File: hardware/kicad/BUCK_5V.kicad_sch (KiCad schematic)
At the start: 0 parts

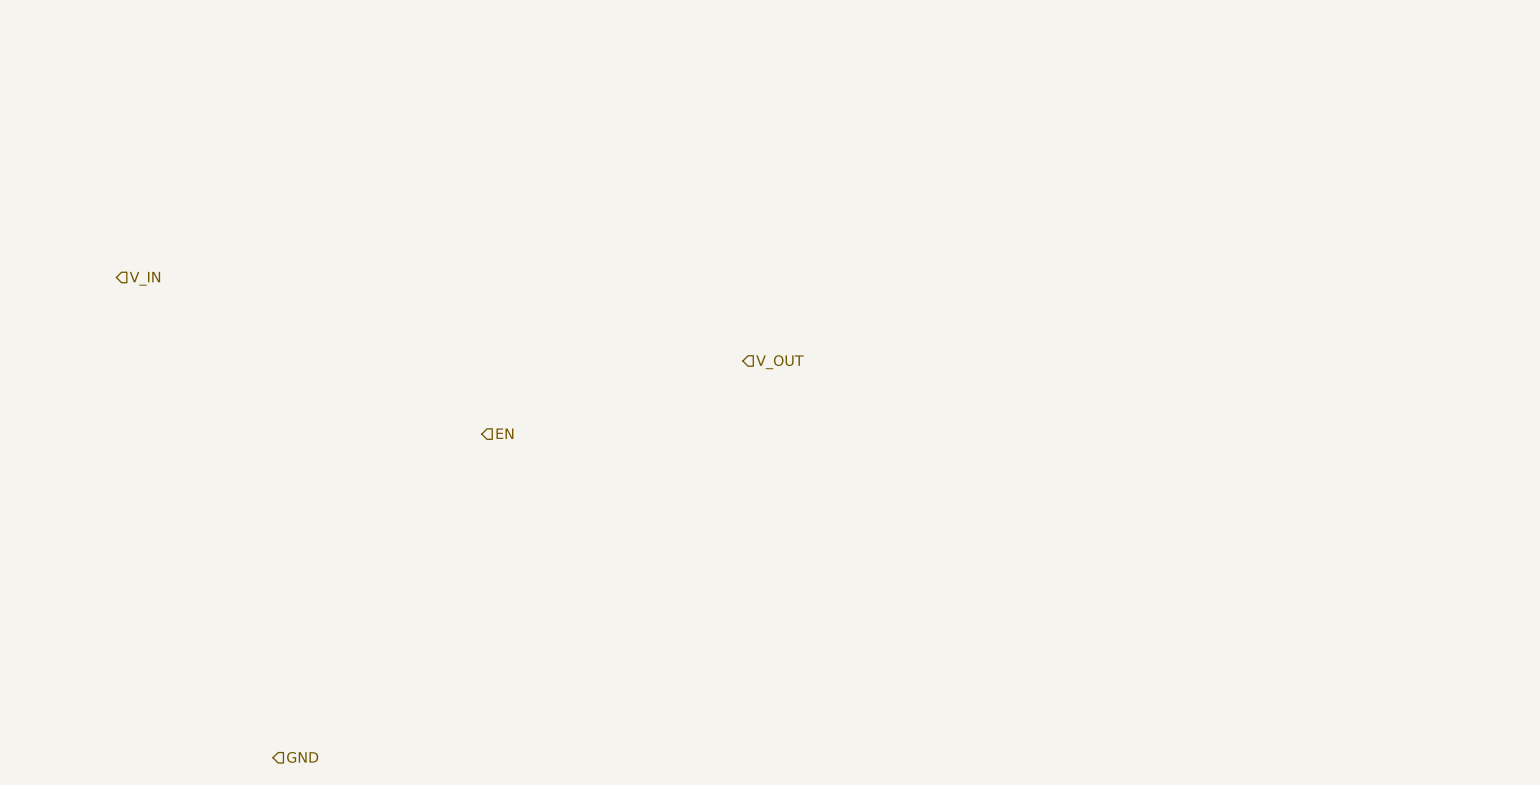
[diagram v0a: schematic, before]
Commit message: feat: added buck 12-5 & 12-3V3 layouts
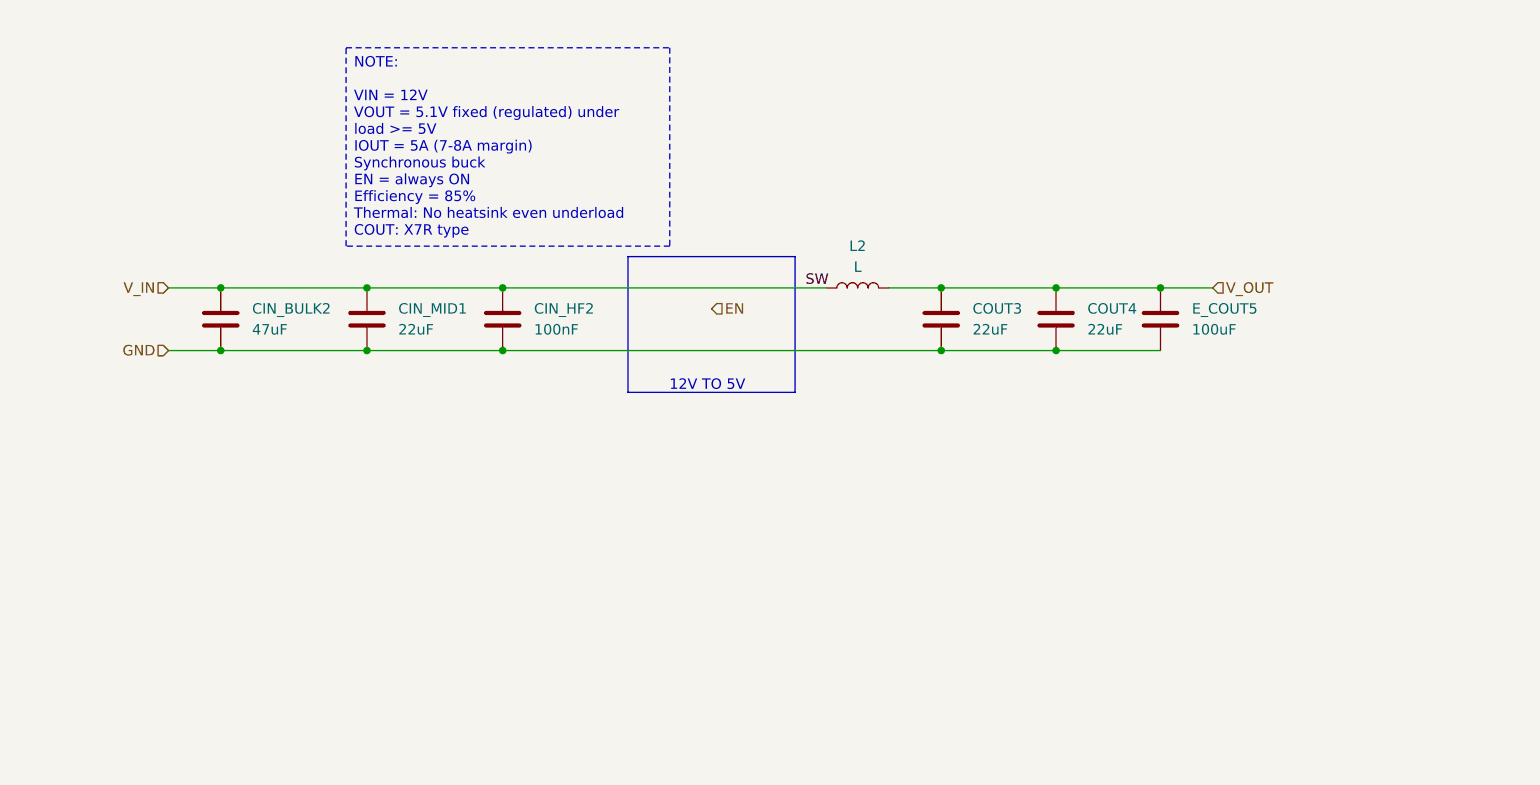
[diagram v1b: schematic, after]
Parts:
- added CIN_BULK2: 47uF, symbol Device:C
- added CIN_HF2: 100nF, symbol Device:C
- added CIN_MID1, COUT3, COUT4: 22uF, symbol Device:C
- added E_COUT5: 100uF, symbol Device:C
- added L2: L, symbol Device:L
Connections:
- net GND: now also CIN_BULK2.2, CIN_HF2.2, CIN_MID1.2, COUT3.2, COUT4.2, E_COUT5.2
- net V_IN: now also CIN_BULK2.1, CIN_HF2.1, CIN_MID1.1, L2.1
- net V_OUT: now also COUT3.1, COUT4.1, E_COUT5.1, L2.2
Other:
- note added: "12V TO 5V"

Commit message: feat: mcu interfaces & motor connections
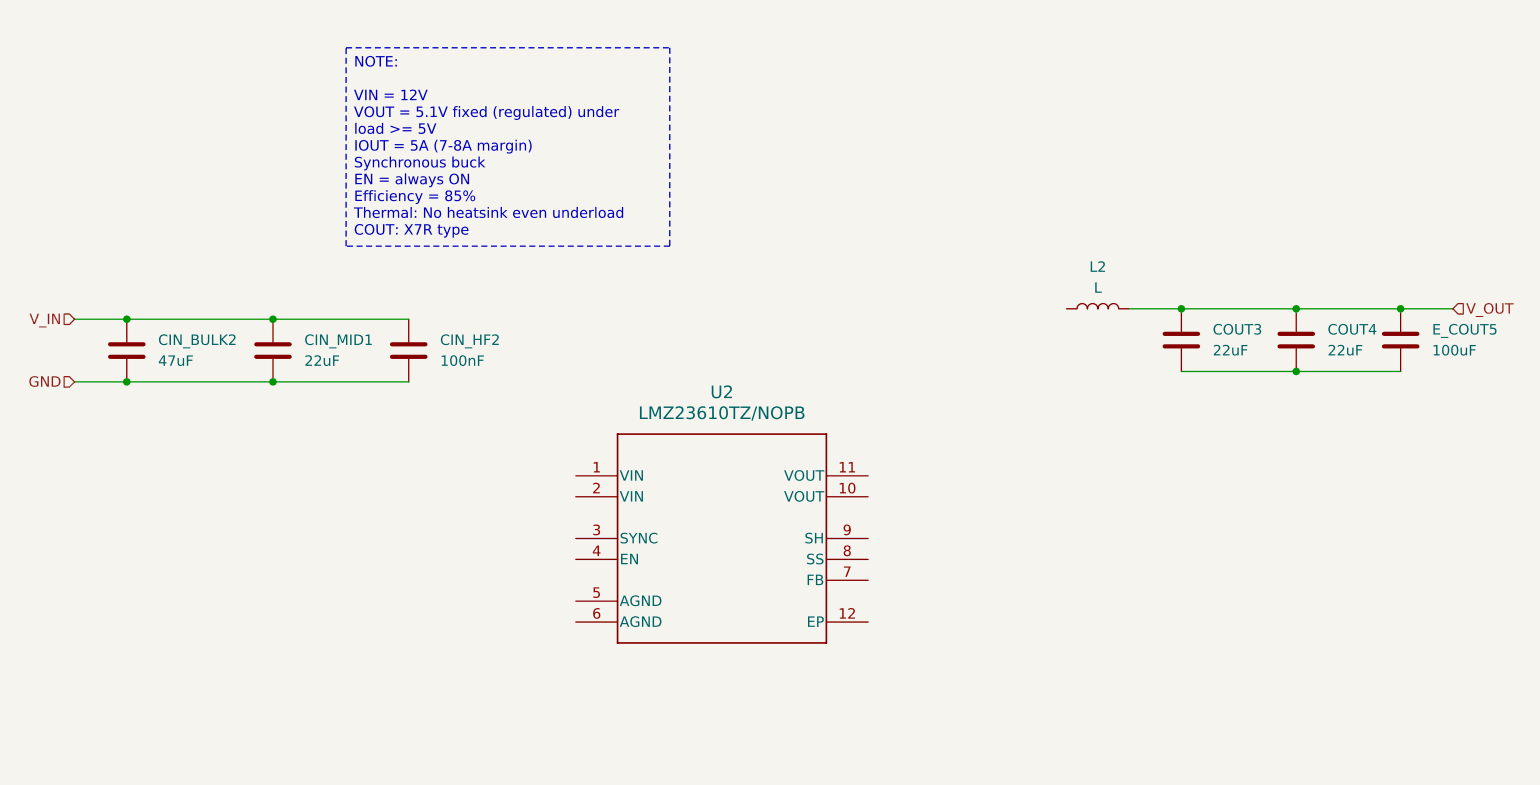
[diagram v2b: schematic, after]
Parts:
- added U2: LMZ23610TZ/NOPB, NDY0011A_N, symbol LMZ23610:LMZ23610TZ_NOPB
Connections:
- net GND: no longer COUT3.2, COUT4.2, E_COUT5.2
- net V_IN: no longer L2.1
- new net: COUT3.2, COUT4.2, E_COUT5.2
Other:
- note removed: "12V TO 5V"
- moved on the sheet: CIN_BULK2, CIN_HF2, CIN_MID1, COUT3, COUT4, E_COUT5, L2

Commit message: fix: error fixing & connection config
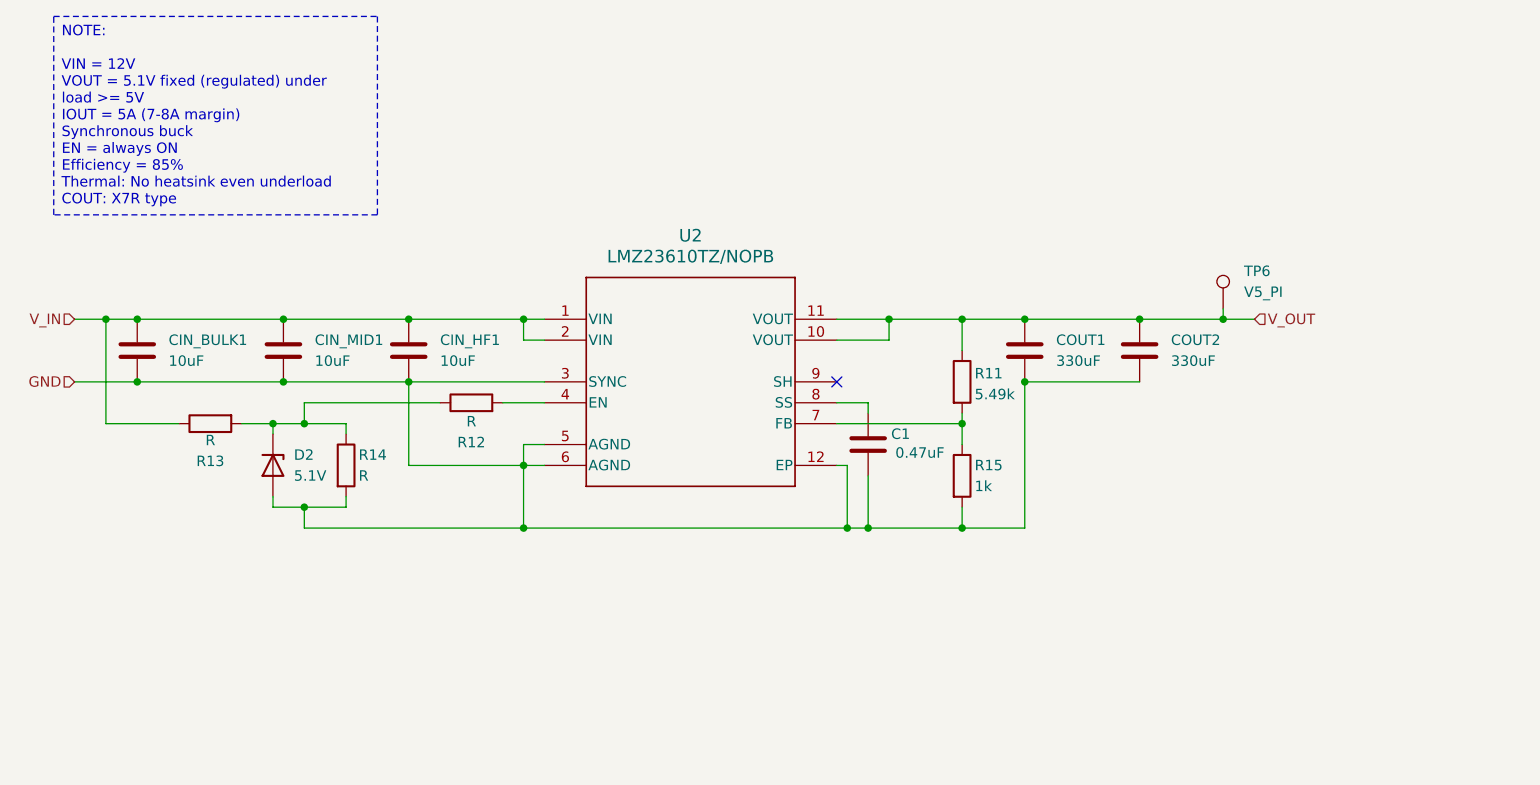
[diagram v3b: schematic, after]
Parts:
- removed E_COUT5: 100uF, symbol Device:C
- removed L2: L, symbol Device:L
- added C1: 0.47uF, symbol Device:C
- added D2: 5.1V, symbol Device:D_Zener
- added R11: 5.49k, symbol Device:R
- added R12, R13, R14: R, symbol Device:R
- added R15: 1k, symbol Device:R
- added TP6: V5_PI, symbol Connector:TestPoint
- CIN_BULK1: renamed from CIN_BULK2; value 47uF -> 10uF
- CIN_HF1: renamed from CIN_HF2; value 100nF -> 10uF
- CIN_MID1: value 22uF -> 10uF
- COUT1: renamed from COUT3; value 22uF -> 330uF
- COUT2: renamed from COUT4; value 22uF -> 330uF
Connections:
- net GND: now also COUT1.2, COUT2.2, U2.12 (EP), U2.3 (SYNC), U2.5 (AGND), U2.6 (AGND), C1.2, D2.2 (A), R14.2, R15.2
- net V_IN: now also U2.1 (VIN), U2.2 (VIN), R13.1
- net V_OUT: now also U2.10 (VOUT), U2.11 (VOUT), R11.1, TP6.1
- net at U2.4 (EN): now also R12.2
- net at U2.7 (FB): now also R11.2, R15.1
- net at U2.8 (SS): now also C1.1
- new net: D2.1 (K), R12.1, R13.2, R14.1
- no-connect marks 0 -> 1
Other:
- moved on the sheet: CIN_BULK1, CIN_MID1, COUT1, COUT2, U2

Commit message: docs: added end semester report for project
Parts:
- C1, CIN_BULK1, CIN_HF1, CIN_MID1, COUT1, COUT2: symbol Device:C -> TPSM82903:C
- D2: symbol Device:D_Zener -> TPSM82903:D_Zener
- R11, R12, R13, R14, R15: symbol Device:R -> TPSM82903:R
- TP6: symbol Connector:TestPoint -> TPSM82903:TestPoint
- U2: symbol LMZ23610:LMZ23610TZ_NOPB -> TPSM82903:LMZ23610TZ_NOPB
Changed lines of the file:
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@@
 	)
 	(symbol
-		(lib_id "Connector:TestPoint")
+		(lib_id "TPSM82903:TestPoint")
 		(at 199.39 81.28 0)
 		(unit 1)
@@
 	)
 	(symbol
-		(lib_id "Device:C")
+		(lib_id "TPSM82903:C")
 		(at 67.31 86.36 0)
 		(unit 1)
@@
 	)
 	(symbol
-		(lib_id "Device:R")
+		(lib_id "TPSM82903:R")
 		(at 76.2 95.25 90)
 		(mirror x)
@@
 	)
 	(symbol
-		(lib_id "Device:C")
+		(lib_id "TPSM82903:C")
 		(at 175.26 86.36 0)
 		(unit 1)
@@
 	)
 	(symbol
-		(lib_id "Device:C")
+		(lib_id "TPSM82903:C")
 		(at 100.33 86.36 0)
 		(unit 1)
@@
 	)
 	(symbol
-		(lib_id "Device:R")
+		(lib_id "TPSM82903:R")
 		(at 92.71 100.33 0)
 		(unit 1)
@@
 	)
 	(symbol
-		(lib_id "Device:C")
+		(lib_id "TPSM82903:C")
 		(at 85.09 86.36 0)
 		(unit 1)
@@
 	)
 	(symbol
-		(lib_id "Device:R")
+		(lib_id "TPSM82903:R")
 		(at 167.64 90.17 0)
 		(unit 1)
@@
 	)
 	(symbol
-		(lib_id "Device:R")
+		(lib_id "TPSM82903:R")
 		(at 107.95 92.71 90)
 		(unit 1)
@@
 	)
 	(symbol
-		(lib_id "Device:D_Zener")
+		(lib_id "TPSM82903:D_Zener")
 		(at 83.82 100.33 270)
 		(unit 1)
@@
 	)
 	(symbol
-		(lib_id "Device:R")
+		(lib_id "TPSM82903:R")
 		(at 167.64 101.6 0)
 		(unit 1)
@@
 	)
 	(symbol
-		(lib_id "Device:C")
+		(lib_id "TPSM82903:C")
 		(at 156.21 97.79 0)
 		(unit 1)
@@
 	)
 	(symbol
-		(lib_id "LMZ23610:LMZ23610TZ_NOPB")
+		(lib_id "TPSM82903:LMZ23610TZ_NOPB")
 		(at 134.62 90.17 0)
 		(unit 1)
@@
 	)
 	(symbol
-		(lib_id "Device:C")
+		(lib_id "TPSM82903:C")
 		(at 189.23 86.36 0)
 		(unit 1)
